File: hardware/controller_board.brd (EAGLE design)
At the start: 144 x 118 mm, 51 parts, among them J1 FRSKY-GIMBAL, J2 FRSKY-GIMBAL, J3 WIRE-HARNESS-SPARKFUN-9915, J4 AVR_SPI_PRG_6NS, J7 FTDI_BASICPTH, U1 ATMEGA128RFA1, U2 TPS73633-DBVT, Y1 CRYSTAL5X3

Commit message: Removed dedicated ground plane for antenna; merged with L2 ground plane; added ground pour on top of the board.  Moved FTDI programming header and mattery connector down.
Updated silkscreen as Rev2.

Updated test code to match new hardware
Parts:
- moved J7 7.63 mm to (24.0, 47.2)
- moved BATT5 7.62 mm to (-58.4, 46.3)
- moved C6 5.10 mm to (25.7, 41.4)
- moved R3 4.98 mm to (23.4, 41.4)
- moved C23 1.75 mm to (-4.50, 34.5), turned to 270 degrees
- moved C22 1.50 mm to (-4.50, 38.2)
- moved Y1 0.75 mm to (-8.00, 36.8)
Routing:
- net VBAT: track 179.6 -> 0.00 mm, vias 1 -> 0
- net GREF: track 175.6 -> 0.00 mm
- net BTN2: track 144.5 -> 0.00 mm, vias 1 -> 0
- net GND: track 139.6 -> 0.00 mm, vias 13 -> 0
- net BTN1: track 114.9 -> 0.00 mm, vias 1 -> 0
- net PITCH: track 102.2 -> 0.00 mm, vias 2 -> 0
- net +3V3: track 102.0 -> 0.00 mm, vias 2 -> 0
- net ROLL: track 97.4 -> 0.00 mm, vias 2 -> 0
- net RESET: track 95.2 -> 0.00 mm, vias 2 -> 0
- net YAW: track 92.4 -> 0.00 mm, vias 1 -> 0
- net POT4: track 90.6 -> 0.00 mm, vias 2 -> 0
- net THROTTLE: track 77.7 -> 0.00 mm, vias 1 -> 0
- net POT3: track 66.3 -> 0.00 mm, vias 1 -> 0
- net POT1: track 60.8 -> 0.00 mm, vias 1 -> 0
- net SCK: track 58.7 -> 0.00 mm, vias 1 -> 0
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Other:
- board text added: "Mark III rev1"
- board text added: "Todo * Run at 3.3V and reconnect FTDI pins and programmer pins. * Add FTDI chip w/ jumper to disable. * Add N-pin connector so you can program the quad with the on-board FTDI * Add Lipo charger. * Use surface-mount power resistor. * More buttons * lower serial display and wrap controller more tightlight around it. * See if we can make the board as narrow as the LCD. Maybe removinng the breakout a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"
- board text removed: "Mark III"
- board text removed: "Todo * lower serial display and wrap controller more tightlight around it. * See if we can make the board as narrow as the LCD. Maybe removinng the breakout area."

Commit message: Remove big caps
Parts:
- removed C2, C7: (no value), KoalaBuild:CAPPRD250W80D630H1220P
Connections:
- net +3V3: no longer C2.1
- net GND: no longer C2.2, C7.2
- net VBAT: no longer C7.1

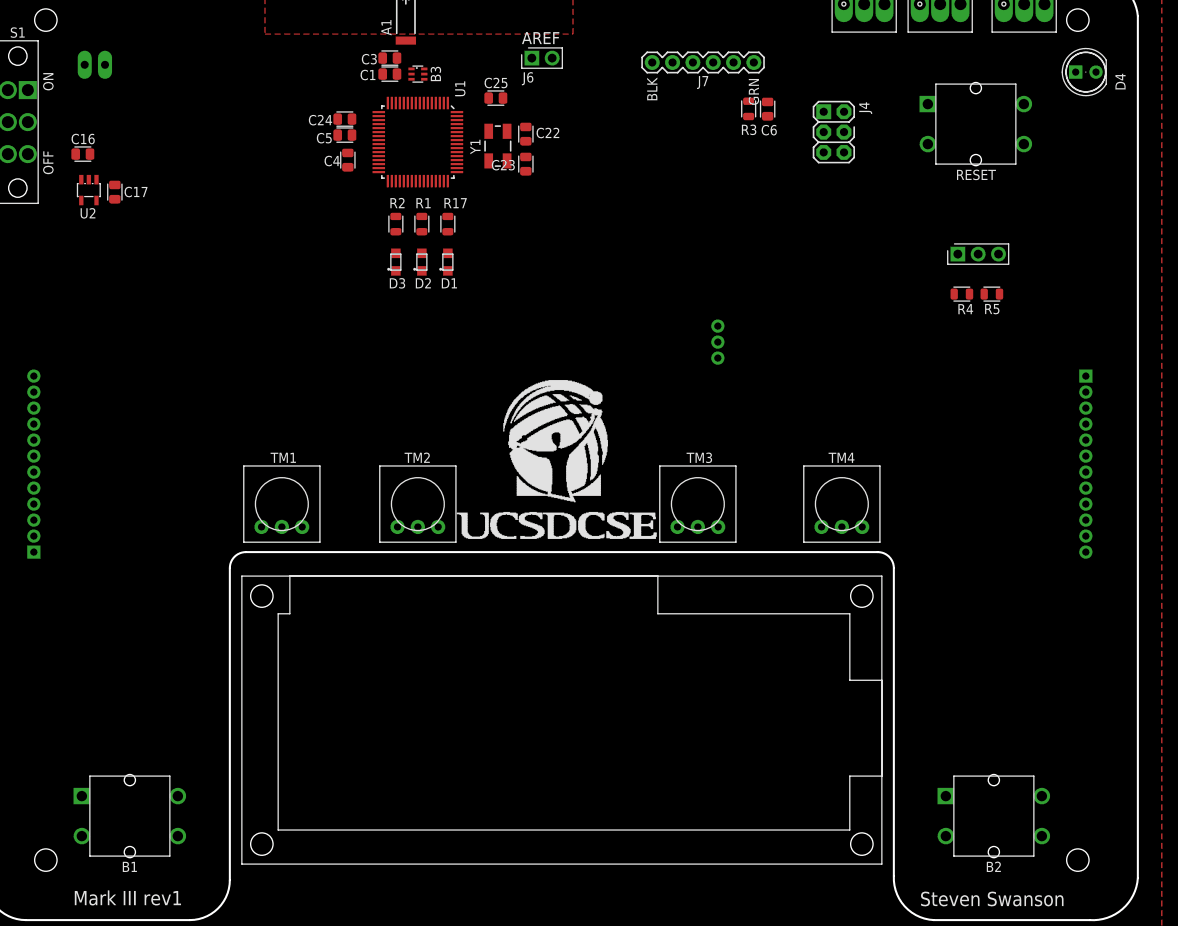
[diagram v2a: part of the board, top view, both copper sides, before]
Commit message: surface mount buttons and power led
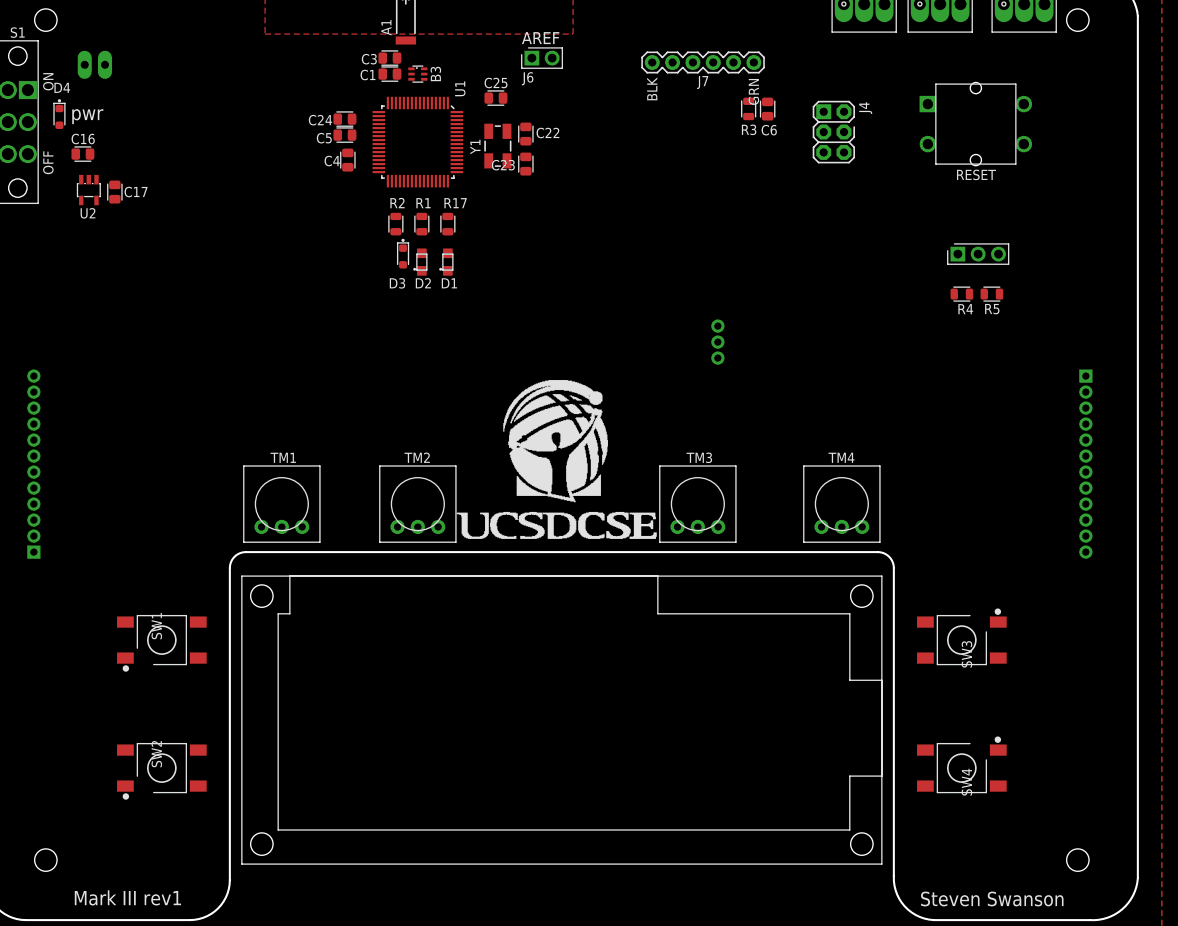
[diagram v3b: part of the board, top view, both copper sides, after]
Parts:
- removed B1, B2: BUTTON-TACTILE-SQUARE, Controller:BUTTON-TACTILE-SQUARE-ADAFRUIT1010
- added SW1, SW2, SW3, SW4: PUSHBUTTON_SMD-VERTICAL-1, quadparts_prebuilt:TE_FSM8JSMA_HS
- D3: value LED-RED -> green; device custom:LED_LTST-C170EKT -> quadparts_prebuilt:LEDSC125X200X120-2_HS
- D4: value (none) -> green; device Components:LED5MM -> quadparts_prebuilt:LEDSC125X200X120-2_HS
- moved D4 129.4 mm to (-63.7, 39.7), turned to 90 degrees
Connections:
- new net BTN3: SW3.3, SW3.4, U1.16
- new net BTN4: SW4.3, SW4.4, U1.17
- net BTN1: now also SW2.3, SW2.4; no longer B1.S, B1.S2
- net BTN2: now also SW1.3, SW1.4; no longer B2.S, B2.S2
- net GND: now also D4.C, SW1.1, SW1.2, SW2.1, SW2.2, SW3.1, SW3.2, SW4.1, SW4.2; no longer B1.P, B1.P2, B2.P, B2.P2, D4.K
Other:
- board text added: "pwr"

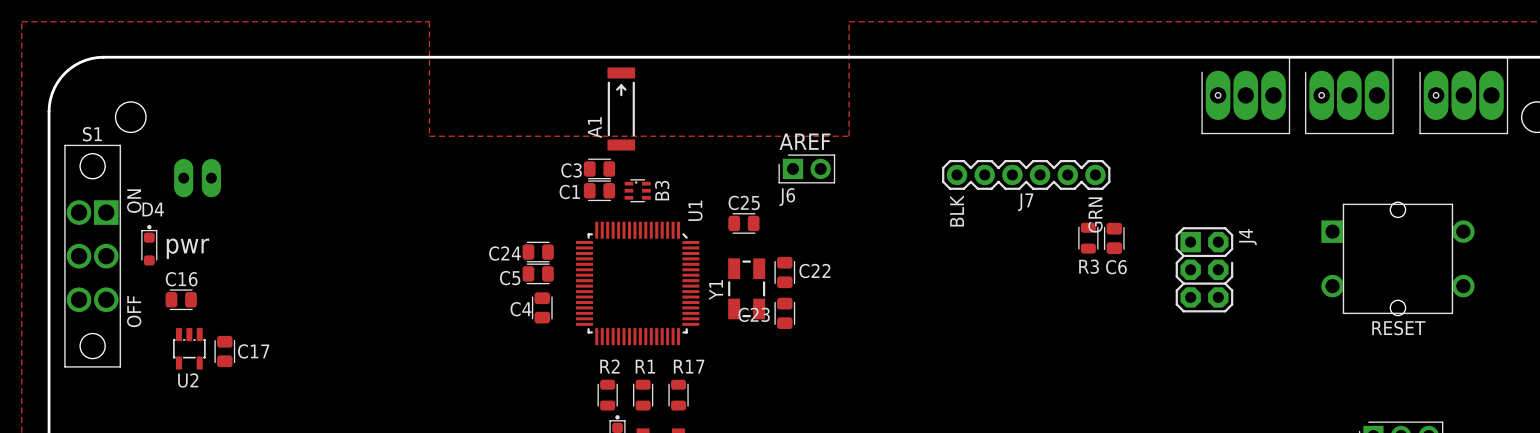
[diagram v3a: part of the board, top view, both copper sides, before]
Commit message: Surface mount power switch
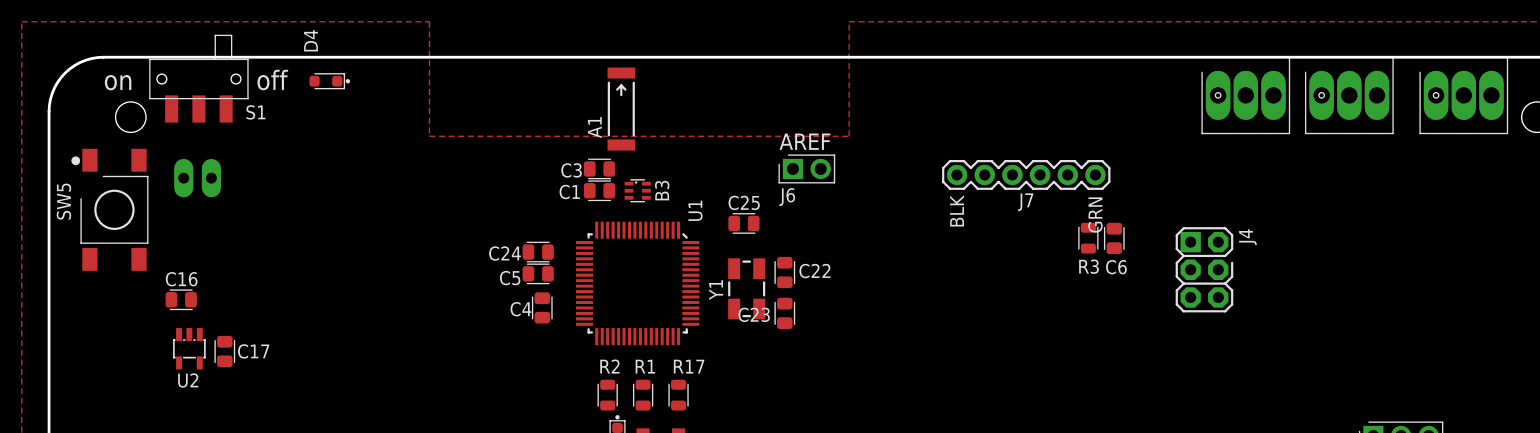
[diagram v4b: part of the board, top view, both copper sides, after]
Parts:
- removed RESET: BUTTON-TACTILE-SQUARE, Controller:BUTTON-TACTILE-SQUARE-ADAFRUIT1010
- added SW5: PUSHBUTTON_SMD-VERTICAL-1, quadparts_prebuilt:TE_FSM8JSMA_HS
- S1: value POWER-SWITCH-MFS201N-9-Z -> POWER-SWITCH-MFS201N-9-ZJS102011SAQN; device RemoteParts:POWER-SWITCH-MFS201N-9-Z -> RemoteParts:JS102011SAQN
- moved D4 23.6 mm to (-47.3, 56.7), turned to 0 degrees
- moved S1 19.0 mm to (-58.2, 56.0), turned to 180 degrees
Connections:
- net GND: now also SW5.3, SW5.4; no longer RESET.S, RESET.S2
- net N$1: no longer S1.P$4
- net RESET: now also SW5.1, SW5.2; no longer RESET.P, RESET.P2
- net VBAT: no longer S1.P$5
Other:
- board text added: "Todo * Run at 3.3V and reconnect FTDI pins and programmer pins. * Add FTDI chip w/ jumper to disable. * Add N-pin connector so you can program the quad with the on-board FTDI * Add Lipo charger. * lower serial display and wrap controller more tightlight around it. * See if we can make the board as narrow as the LCD. Maybe removinng the breakout area."
- board text added: "off"
- board text added: "on"
- board text removed: "Todo * Run at 3.3V and reconnect FTDI pins and programmer pins. * Add FTDI chip w/ jumper to disable. * Add N-pin connector so you can program the quad with the on-board FTDI * Add Lipo charger. * Use surface-mount power resistor. * More buttons * lower serial display and wrap controller more tightlight around it. * See if we can make the board as narrow as the LCD. Maybe removinng the breakout a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"
- board text removed: "pwr"
